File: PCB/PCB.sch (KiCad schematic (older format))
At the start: 186 parts, among them K0,0 KEYSW, K0,1 KEYSW, K0,10 KEYSW, K0,11 KEYSW, K0,12 KEYSW, K0,13 KEYSW, K0,14 KEYSW, K0,15 KEYSW, K0,16 KEYSW, K0,17 KEYSW, K0,18 KEYSW, K0,19 KEYSW, K0,2 KEYSW, K0,20 KEYSW, K0,3 KEYSW, K0,4 KEYSW, K0,5 KEYSW, K0,6 KEYSW, K0,7 KEYSW, K0,8 KEYSW, K0,9 KEYSW, K1,0 KEYSW, K1,1 KEYSW, K1,10 KEYSW, K1,11 KEYSW, K1,12 KEYSW, K1,13 KEYSW, K1,14 KEYSW, K1,15 KEYSW, K1,16 KEYSW, K1,17 KEYSW, K1,18 KEYSW, K1,19 KEYSW, K1,2 KEYSW, K1,20 KEYSW, K1,3 KEYSW, K1,4 KEYSW, K1,5 KEYSW, K1,6 KEYSW, K1,7 KEYSW, K1,8 KEYSW, K1,9 KEYSW, K2,0 KEYSW, K2,1 KEYSW, K2,10 KEYSW, K2,11 KEYSW, K2,12 KEYSW, K2,13 KEYSW, K2,14 KEYSW, K2,15 KEYSW, K2,17 KEYSW, K2,18 KEYSW, K2,19 KEYSW, K2,2 KEYSW, K2,20 KEYSW, K2,4 KEYSW, K2,5 KEYSW, K2,6 KEYSW, K2,7 KEYSW, K2,8 KEYSW, K2,9 KEYSW, K3,0 KEYSW, K3,1 KEYSW, K3,10 KEYSW, K3,11 KEYSW, K3,12 KEYSW, K3,13 KEYSW, K3,14 KEYSW, K3,17 KEYSW, K3,18 KEYSW, K3,19 KEYSW, K3,2 KEYSW, K3,20 KEYSW, K3,3 KEYSW, K3,4 KEYSW, K3,5 KEYSW, K3,6 KEYSW, K3,7 KEYSW, K3,8 KEYSW, K3,9 KEYSW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

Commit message: Oriented diodes; laid down MCU and BT module
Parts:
- added C1, C2: 22p, symbol C_Small
- added IC1: ATXMEGA64C3-A, TQFP64, symbol ATXMEGA64C3-A
- added RB1: 3.3k, symbol R
- added RB2: 3,3k, symbol R
- added U1: RN42, symbol RN42
- added X1: XTAL_GND, symbol XTAL_GND
- renumbered D3,17 to D3,16, K3,17 to K3,16
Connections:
- net labels added: GND
- wire segments 212 -> 246
- no-connect marks 0 -> 7
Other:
- moved on the sheet: D3,16, K3,16

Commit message: Switched MCUs; removed BT for now
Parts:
- removed IC1: ATXMEGA64C3-A, TQFP64, symbol ATXMEGA64C3-A
- removed RB1: 3.3k, symbol R
- removed RB2: 3,3k, symbol R
- removed U1: RN42, symbol RN42
- added C3, C4, C5: 0.1u, Capacitors_SMD:C_0805_HandSoldering, symbol C_Small
- added C7: 4.7u, Capacitors_SMD:C_0805_HandSoldering, symbol C_Small
- added CU1: 1u, Capacitors_SMD:C_0805_HandSoldering, symbol C_Small
- added J1: USB_mini_micro_B, keyboard_parts:USB_miniB_hirose_5S8, symbol USB_mini_micro_B
- added RR1, RR2: 10k, Resistors_SMD:R_0805_HandSoldering, symbol R
- added RU1, RU2: 22, Resistors_SMD:R_0805_HandSoldering, symbol R
- added SW1: SW_PUSH, Buttons_Switches_SMD:SW_SPST_TL3342, symbol SW_PUSH
- added U1: AT90USB1286, Housings_QFP:TQFP-64_14x14mm_Pitch0.8mm, symbol AT90USB1286
- C1, C2: footprint (none) -> Capacitors_SMD:C_0805_HandSoldering
- X1: footprint (none) -> Crystals:crystal_FA238-TSX3225
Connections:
- net labels added: VCC
- wire segments 246 -> 247
- no-connect marks 7 -> 23
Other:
- moved on the sheet: C1, C2, D0,0, D0,1, D0,10, D0,11, D0,12, D0,13, D0,14, D0,15, D0,16, D0,17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

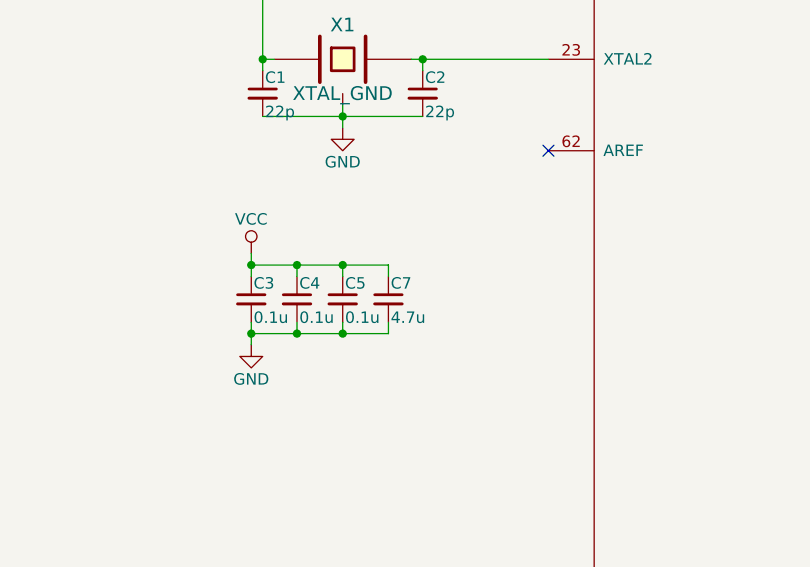
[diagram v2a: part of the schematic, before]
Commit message: USB routed and most components connected
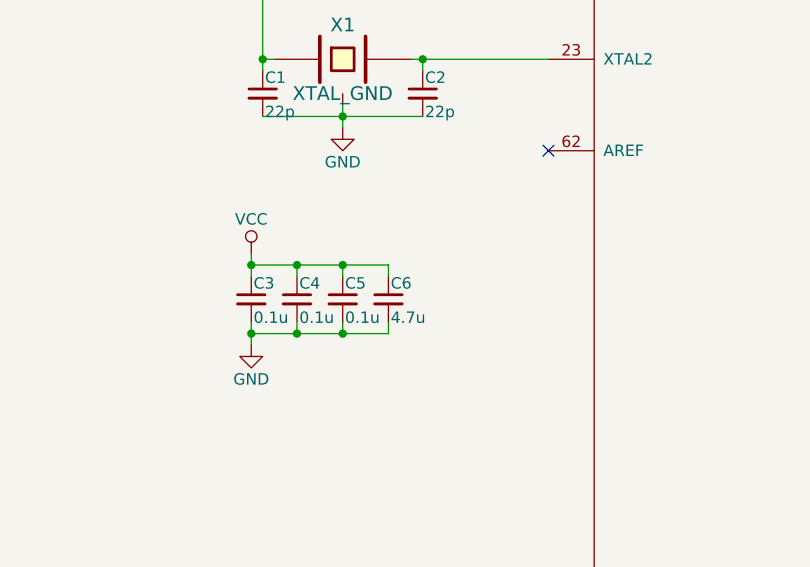
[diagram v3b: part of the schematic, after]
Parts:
- renumbered C7 to C6
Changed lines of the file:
@@
 $EndComp
 $Comp
-L C_Small C7
+L C_Small C6
 U 1 1 58A456F4
 P 9150 10200
-F 0 "C7" H 9160 10270 50  0000 L CNN
+F 0 "C6" H 9160 10270 50  0000 L CNN
 F 1 "4.7u" H 9160 10120 50  0000 L CNN
 F 2 "Capacitors_SMD:C_0805_HandSoldering" H 9150 10200 50  0001 C CNN

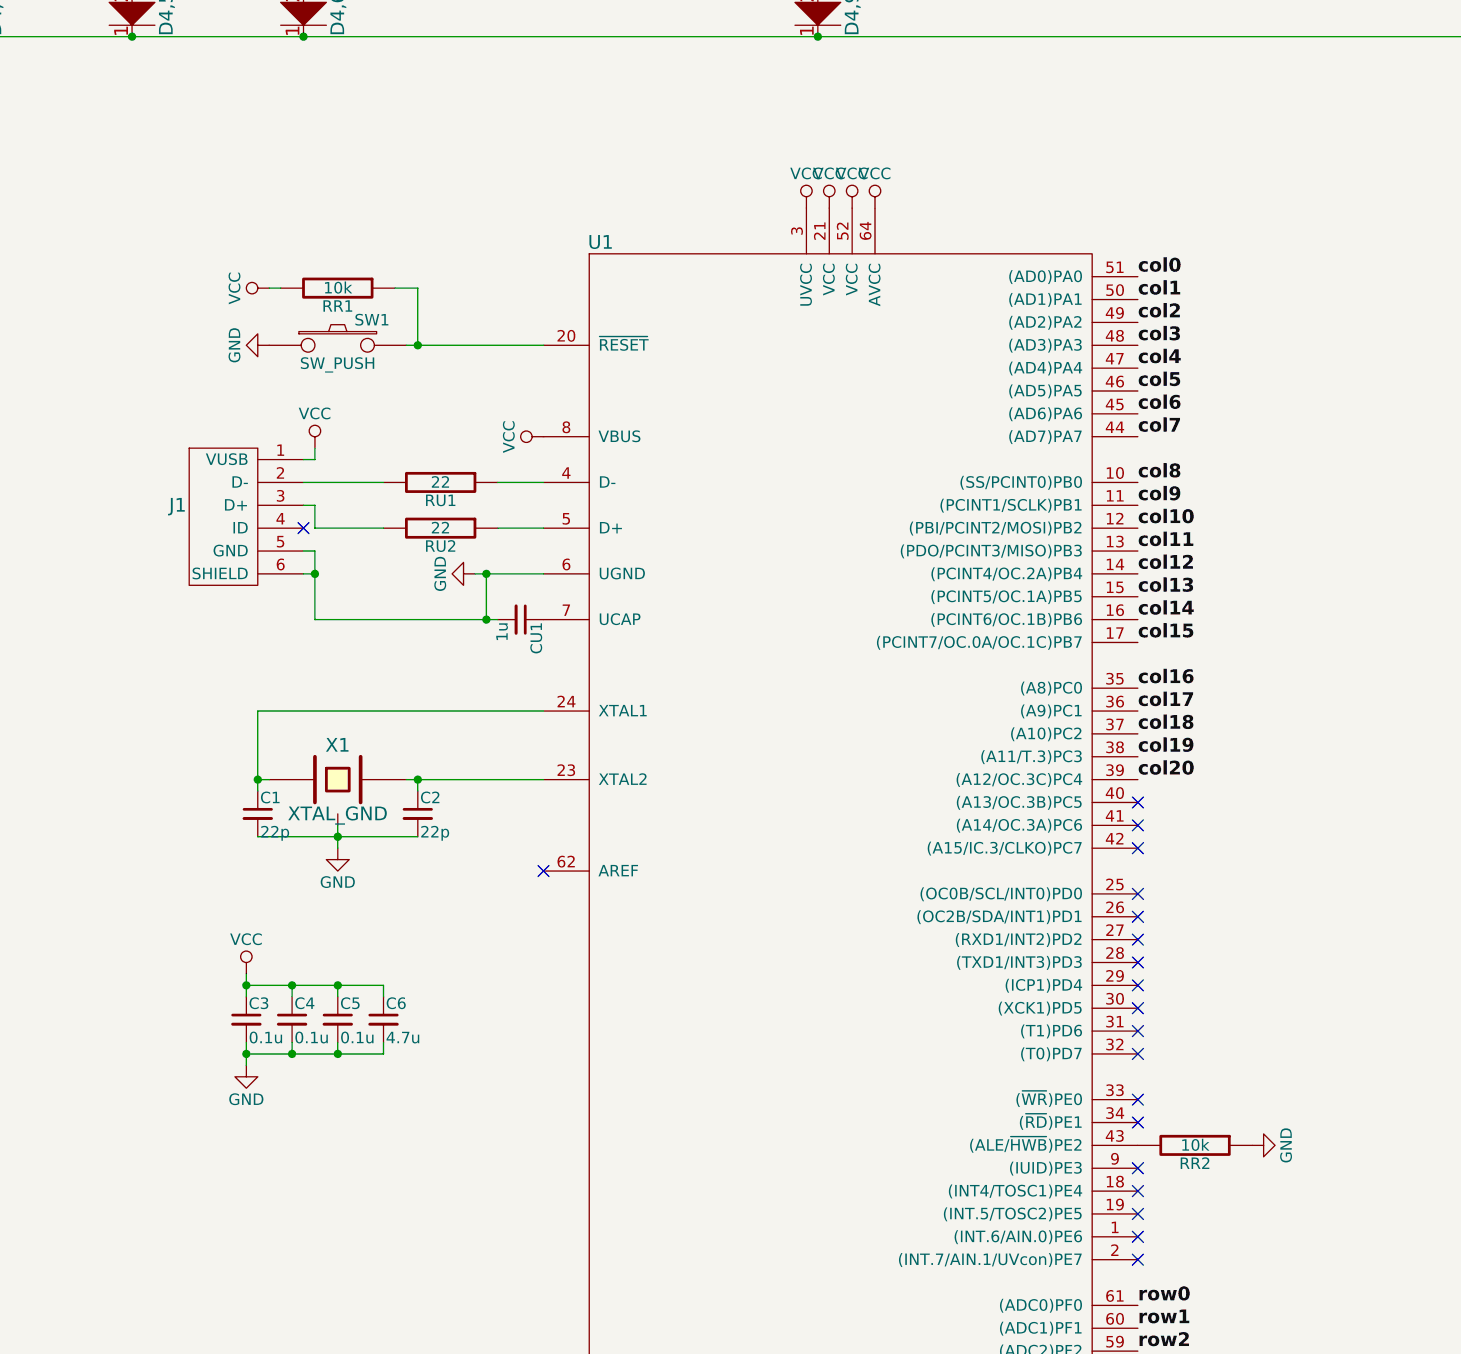
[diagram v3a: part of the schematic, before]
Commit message: Redid the layout to resemble the Teensy++ 2.0 more
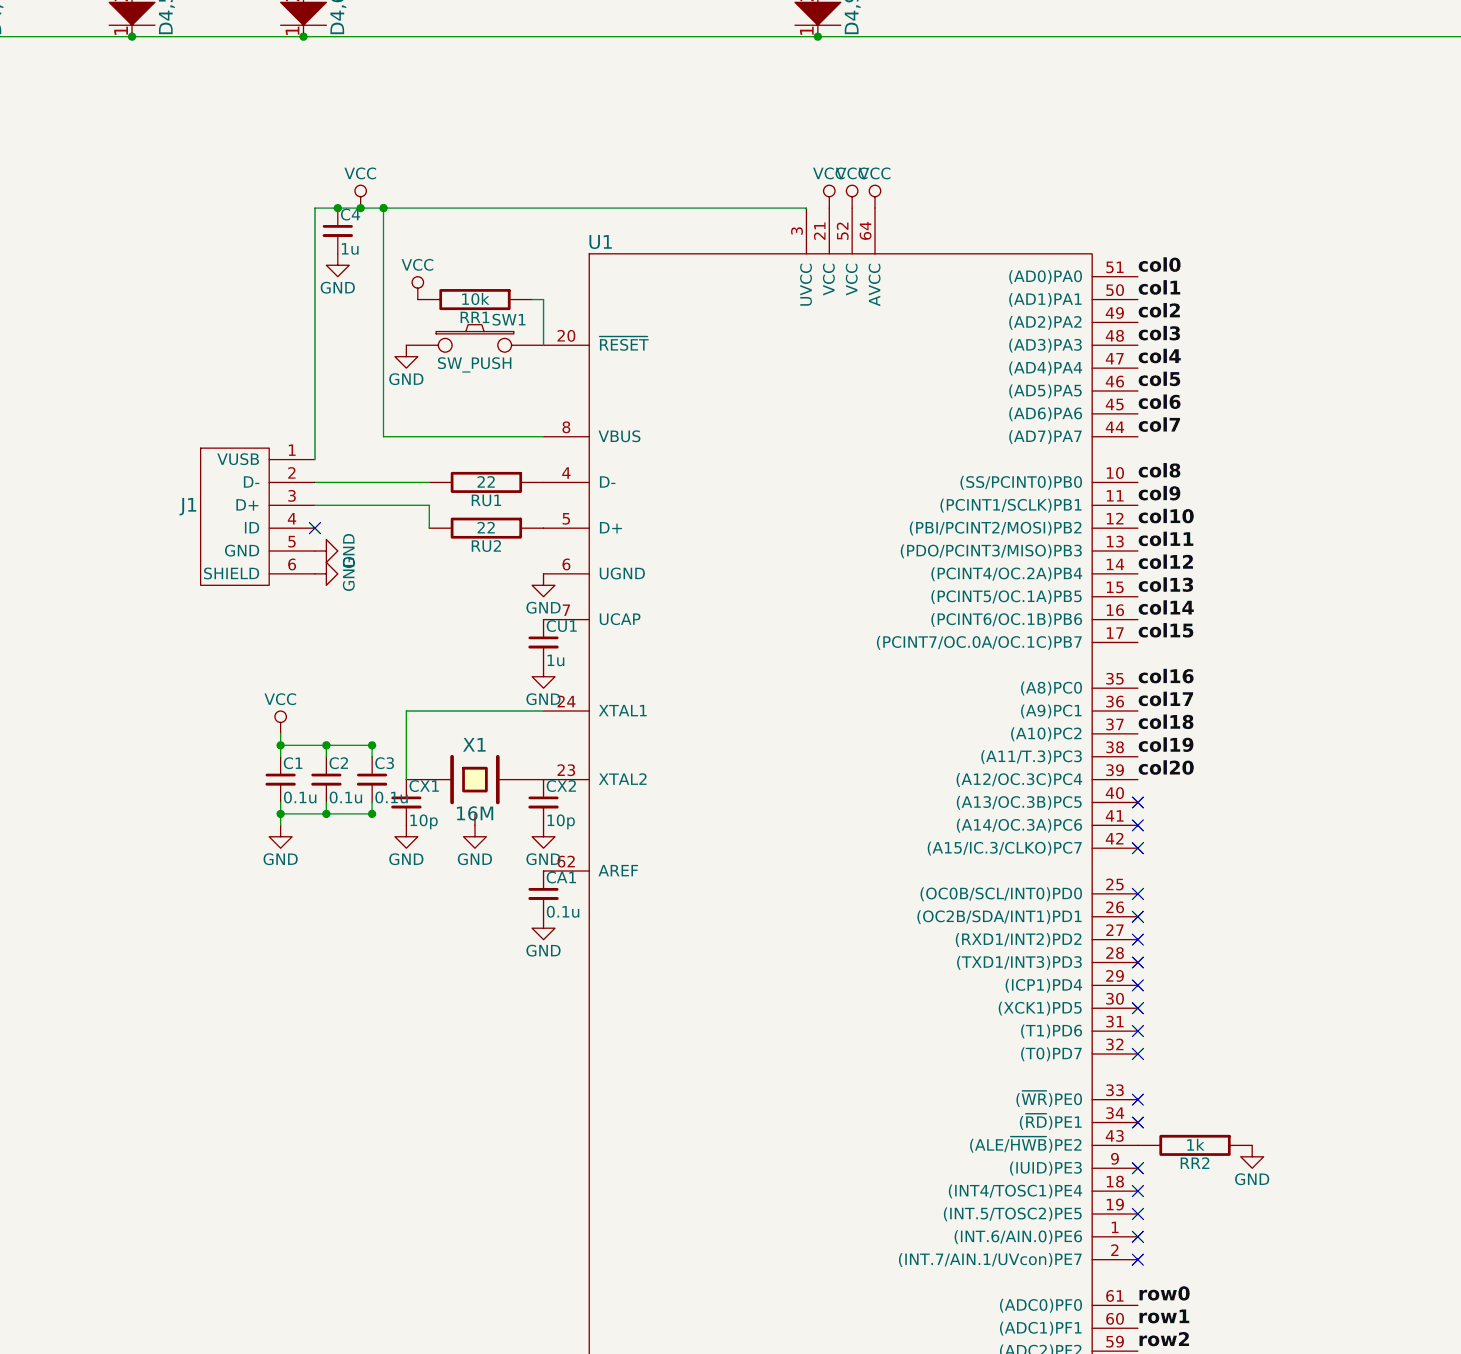
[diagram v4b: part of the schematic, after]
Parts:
- added CA1: 0.1u, Capacitors_SMD:C_0805_HandSoldering, symbol C_Small
- C4: renamed from C6; value 4.7u -> 1u
- CX1: renamed from C1; value 22p -> 10p
- CX2: renamed from C2; value 22p -> 10p
- RR2: value 10k -> 1k
- X1: value XTAL_GND -> 16M; footprint Crystals:crystal_FA238-TSX3225 -> keyboard_parts:FA-238
- renumbered C3 to C1, C4 to C2, C5 to C3
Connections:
- net GND: now also CA1.2
- net at U1.62 (AREF): now also CA1.1
- no-connect marks 23 -> 22
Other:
- moved on the sheet: C1, C2, C3, C4, CU1, CX1, CX2, J1, RR1, RU1, RU2, SW1

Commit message: Taking new design approach; updated submodules
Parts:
- removed C1, C2, C3, CA1: 0.1u, Capacitors_SMD:C_0805_HandSoldering, symbol C_Small
- removed C4, CU1: 1u, Capacitors_SMD:C_0805_HandSoldering, symbol C_Small
- removed CX1, CX2: 10p, Capacitors_SMD:C_0805_HandSoldering, symbol C_Small
- removed J1: USB_mini_micro_B, keyboard_parts:USB_miniB_hirose_5S8, symbol USB_mini_micro_B
- removed RR1: 10k, Resistors_SMD:R_0805_HandSoldering, symbol R
- removed RR2: 1k, Resistors_SMD:R_0805_HandSoldering, symbol R
- removed RU1, RU2: 22, Resistors_SMD:R_0805_HandSoldering, symbol R
- removed SW1: SW_PUSH, Buttons_Switches_SMD:SW_SPST_TL3342, symbol SW_PUSH
- removed U1: AT90USB1286, Housings_QFP:TQFP-64_14x14mm_Pitch0.8mm, symbol AT90USB1286
- removed X1: 16M, keyboard_parts:FA-238, symbol XTAL_GND
- added U1: Teensy2.0++, keebs:Teensy_20, symbol Teensy2.0++
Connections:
- net col0: now also U1.21 (PF7)
- net col1: now also U1.22 (PF6)
- net col10: now also U1.35 (PB2)
- net col11: now also U1.36 (PB3)
- net col12: now also U1.37 (PB4)
- net col13: now also U1.38 (PB5)
- net col14: now also U1.39 (PB6)
- net col15: now also U1.1 (PB7)
- net col16: now also U1.3 (PD0)
- net col17: now also U1.4 (PD1)
- net col18: now also U1.5 (PD2)
- net col19: now also U1.6 (PD3)
- net col2: now also U1.23 (PF5)
- net col20: now also U1.7 (PD4)
- net col3: now also U1.24 (PF4)
- net col4: now also U1.25 (PF3)
- net col5: now also U1.26 (PF2)
- net col6: now also U1.27 (PF1)
- net col7: now also U1.28 (PF0)
- net col8: now also U1.33 (PB0)
- net col9: now also U1.34 (PB1)
- net row0: now also U1.13 (PC0)
- net row1: now also U1.14 (PC1)
- net row2: now also U1.15 (PC2)
- net row3: now also U1.16 (PC3)
- net row4: now also U1.17 (PC4)
- no-connect marks 22 -> 28

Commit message: 2017.11.08 Update
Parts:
- removed U1: Teensy2.0++, keebs:Teensy_20, symbol Teensy2.0++
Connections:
- no-connect marks 28 -> 0
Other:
- moved on the sheet: D0,0, D0,1, D0,10, D0,11, D0,12, D0,13, D0,14, D0,15, D0,16, D0,17, D0,18, D0,19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
